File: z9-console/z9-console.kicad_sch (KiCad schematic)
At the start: 4 parts

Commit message: x
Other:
- sheet buzzer: file ../z9-shared/buzzer.kicad_sch -> ../z9-shared/shared_buzzer.kicad_sch
- sheet usbc: file ../z9-shared/usbc.kicad_sch -> ../z9-shared/shared_usbc.kicad_sch
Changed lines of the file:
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@@
 			)
 		)
-		(property "Sheetfile" "../z9-shared/buzzer.kicad_sch"
+		(property "Sheetfile" "../z9-shared/shared_buzzer.kicad_sch"
 			(at 299.72 85.6746 0)
 			(effects
@@
 			)
 		)
-		(property "Sheetfile" "../z9-shared/usbc.kicad_sch"
+		(property "Sheetfile" "../z9-shared/shared_usbc.kicad_sch"
 			(at 299.72 174.5746 0)
 			(effects

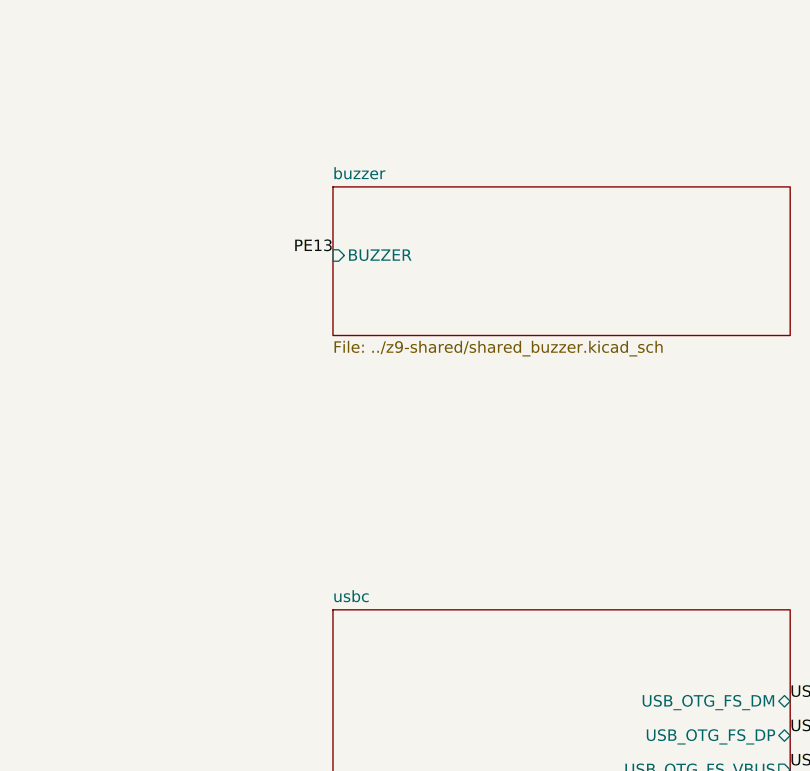
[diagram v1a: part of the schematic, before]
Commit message: lcd power switch-- add new accelerometer
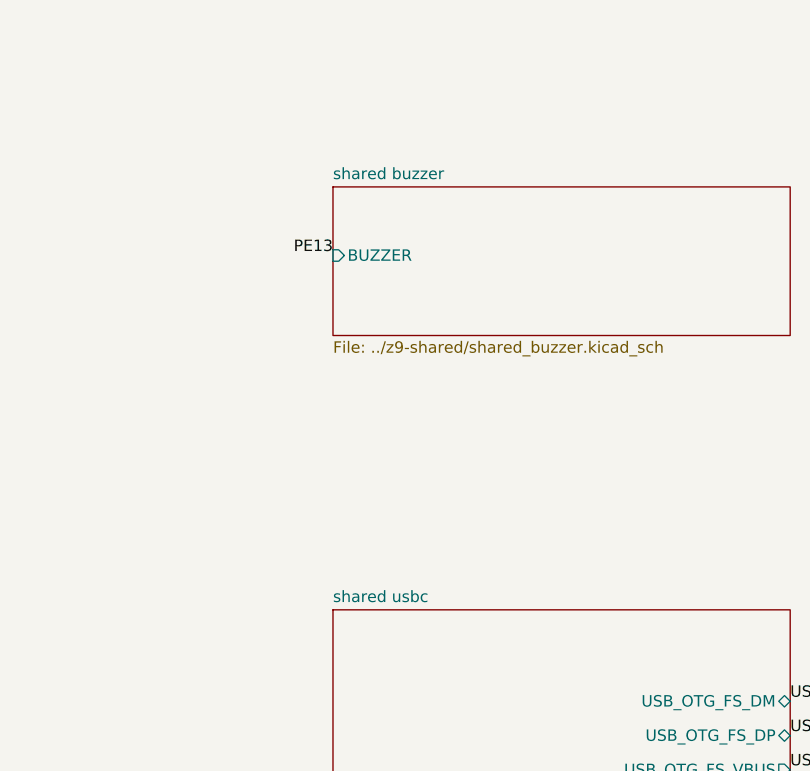
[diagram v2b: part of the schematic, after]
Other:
- sheet buzzer renamed shared buzzer
- sheet usbc renamed shared usbc
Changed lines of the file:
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@@
 			(color 0 0 0 0.0000)
 		)
-		(property "Sheetname" "buzzer"
+		(property "Sheetname" "shared buzzer"
 			(at 299.72 67.8684 0)
 			(effects
@@
 			(color 0 0 0 0.0000)
 		)
-		(property "Sheetname" "usbc"
+		(property "Sheetname" "shared usbc"
 			(at 299.72 114.8584 0)
 			(effects

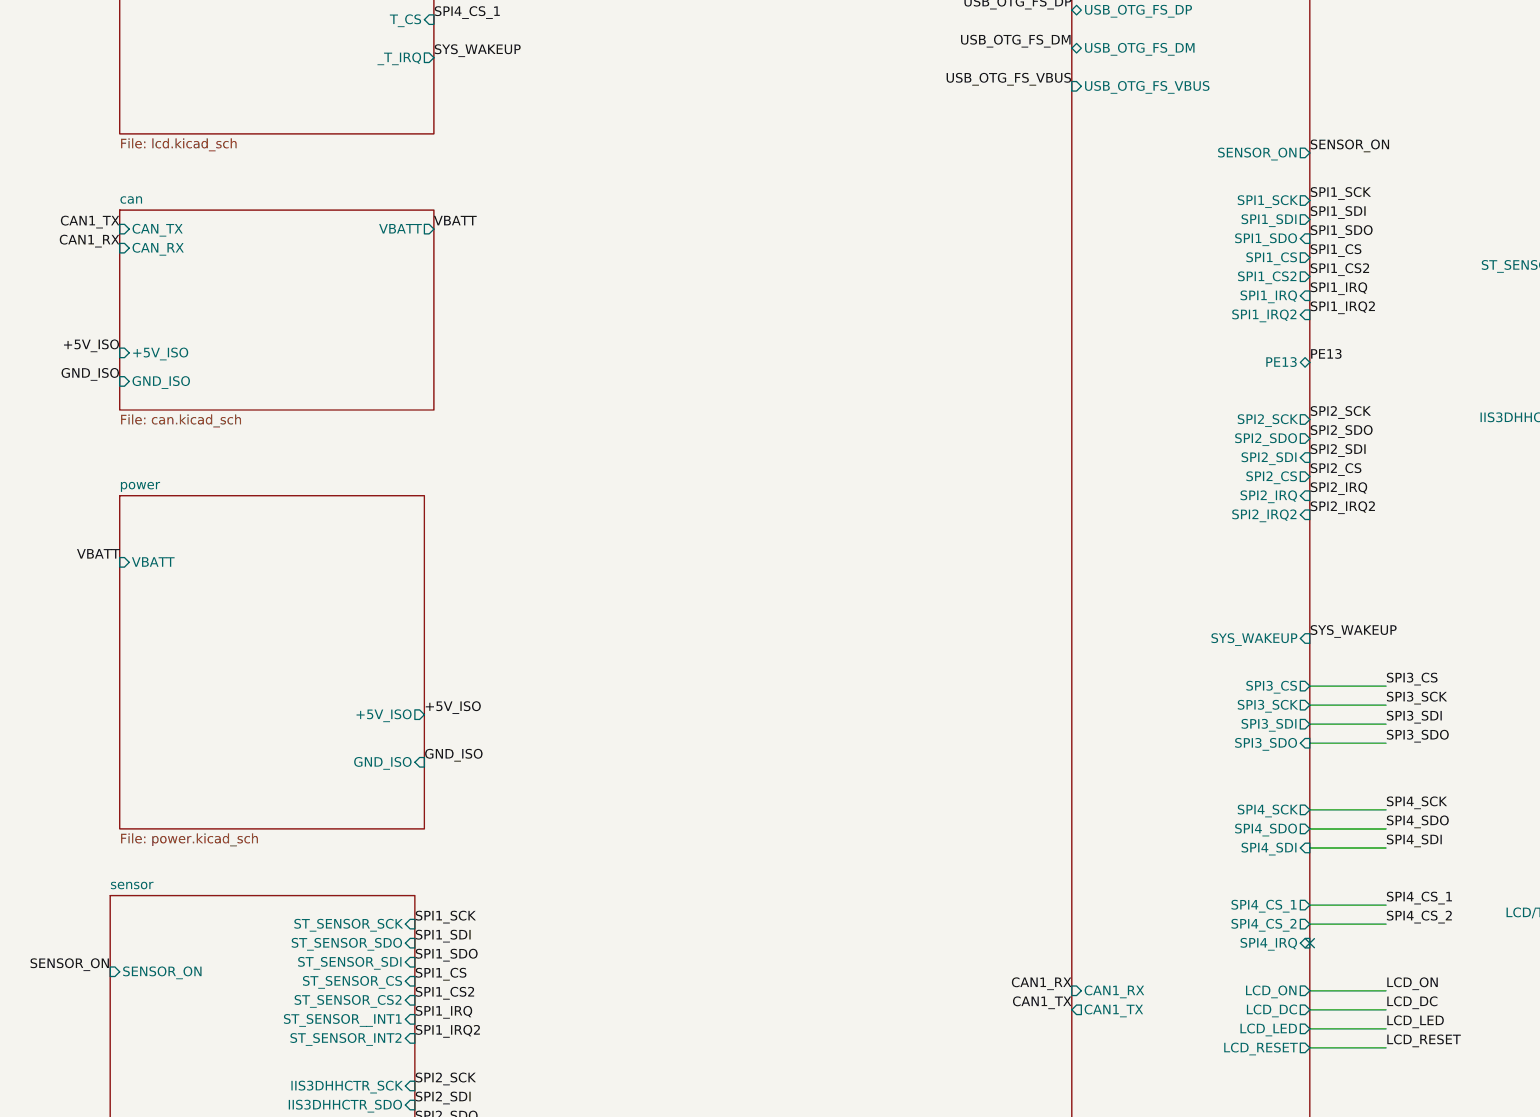
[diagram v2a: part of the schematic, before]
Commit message: change MEMS device
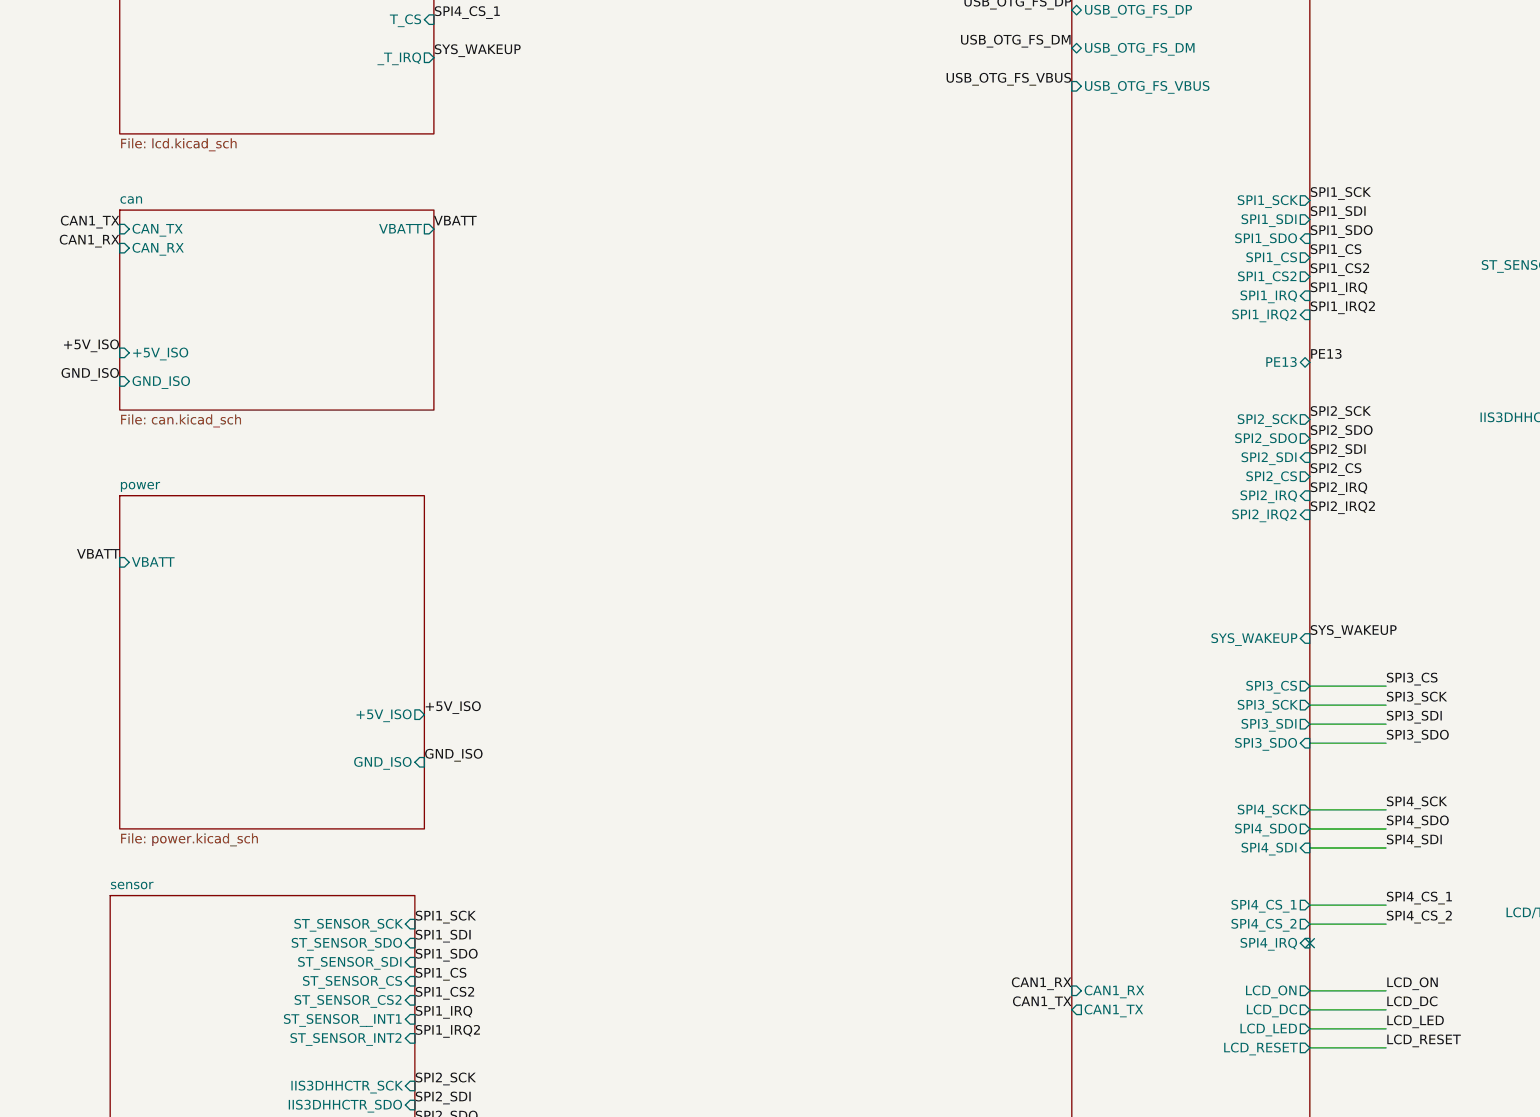
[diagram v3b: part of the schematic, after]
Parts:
- renumbered H2 to H901, H3 to H902, H1 to H903, H4 to H904
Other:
- sheet MCU ports: added none; removed SENSOR_ON
- sheet sensor ports: added none; removed SENSOR_ON
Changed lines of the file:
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@@
-		)
-	)
-	(label "SENSOR_ON"
-		(at 212.09 113.03 0)
-		(effects
-			(font
-				(size 1.27 1.27)
-			)
-			(justify left bottom)
 		)
 	)
@@
 		)
 	)
-	(label "SENSOR_ON"
-		(at 52.07 222.25 180)
-		(effects
-			(font
-				(size 1.27 1.27)
-			)
-			(justify right bottom)
-		)
-	)
 	(label "SPI1_SCK"
 		(at 212.09 119.38 0)
@@
 	)
 	(symbol
-		(lib_name "MountingHole_3")
 		(lib_id "Mechanical:MountingHole")
 		(at 388.62 245.11 0)
@@
 		(dnp no)
 		(fields_autoplaced yes)
-		(property "Reference" "H2"
+		(property "Reference" "H901"
 			(at 391.16 243.8399 0)
 			(effects
@@
 			(project "l8-kicad"
 				(path "/8d063f79-9282-4820-bcf4-1ff3c006cf08"
-					(reference "H2")
+					(reference "H901")
 					(unit 1)
 				)
@@
 	)
 	(symbol
-		(lib_name "MountingHole_1")
 		(lib_id "Mechanical:MountingHole")
 		(at 393.7 245.11 0)
@@
 		(dnp no)
 		(fields_autoplaced yes)
-		(property "Reference" "H3"
+		(property "Reference" "H902"
 			(at 396.24 243.8399 0)
 			(effects
@@
 			(project "l8-kicad"
 				(path "/8d063f79-9282-4820-bcf4-1ff3c006cf08"
-					(reference "H3")
+					(reference "H902")
 					(unit 1)
 				)
@@
 	)
 	(symbol
-		(lib_name "MountingHole_2")
 		(lib_id "Mechanical:MountingHole")
 		(at 398.78 245.11 0)
@@
 		(dnp no)
 		(fields_autoplaced yes)
-		(property "Reference" "H1"
+		(property "Reference" "H903"
 			(at 401.32 243.8399 0)
 			(effects
@@
 			(project "l8-kicad"
 				(path "/8d063f79-9282-4820-bcf4-1ff3c006cf08"
-					(reference "H1")
+					(reference "H903")
 					(unit 1)
 				)
@@
 		(dnp no)
 		(fields_autoplaced yes)
-		(property "Reference" "H4"
+		(property "Reference" "H904"
 			(at 406.4 243.8399 0)
 			(effects
@@
 			(project "l8-kicad"
 				(path "/8d063f79-9282-4820-bcf4-1ff3c006cf08"
-					(reference "H4")
+					(reference "H904")
 					(unit 1)
 				)
@@
 			)
 		)
-		(pin "SENSOR_ON" output
-			(at 212.09 113.03 0)
-			(effects
-				(font
-					(size 1.27 1.27)
-				)
-				(justify right)
-			)
-		)
 		(pin "LCD_DC" output
 			(at 212.09 227.33 0)
@@
 			)
 		)
-		(pin "SENSOR_ON" input
-			(at 52.07 222.25 180)
-			(effects
-				(font
-					(size 1.27 1.27)
-				)
-				(justify left)
-			)
-		)

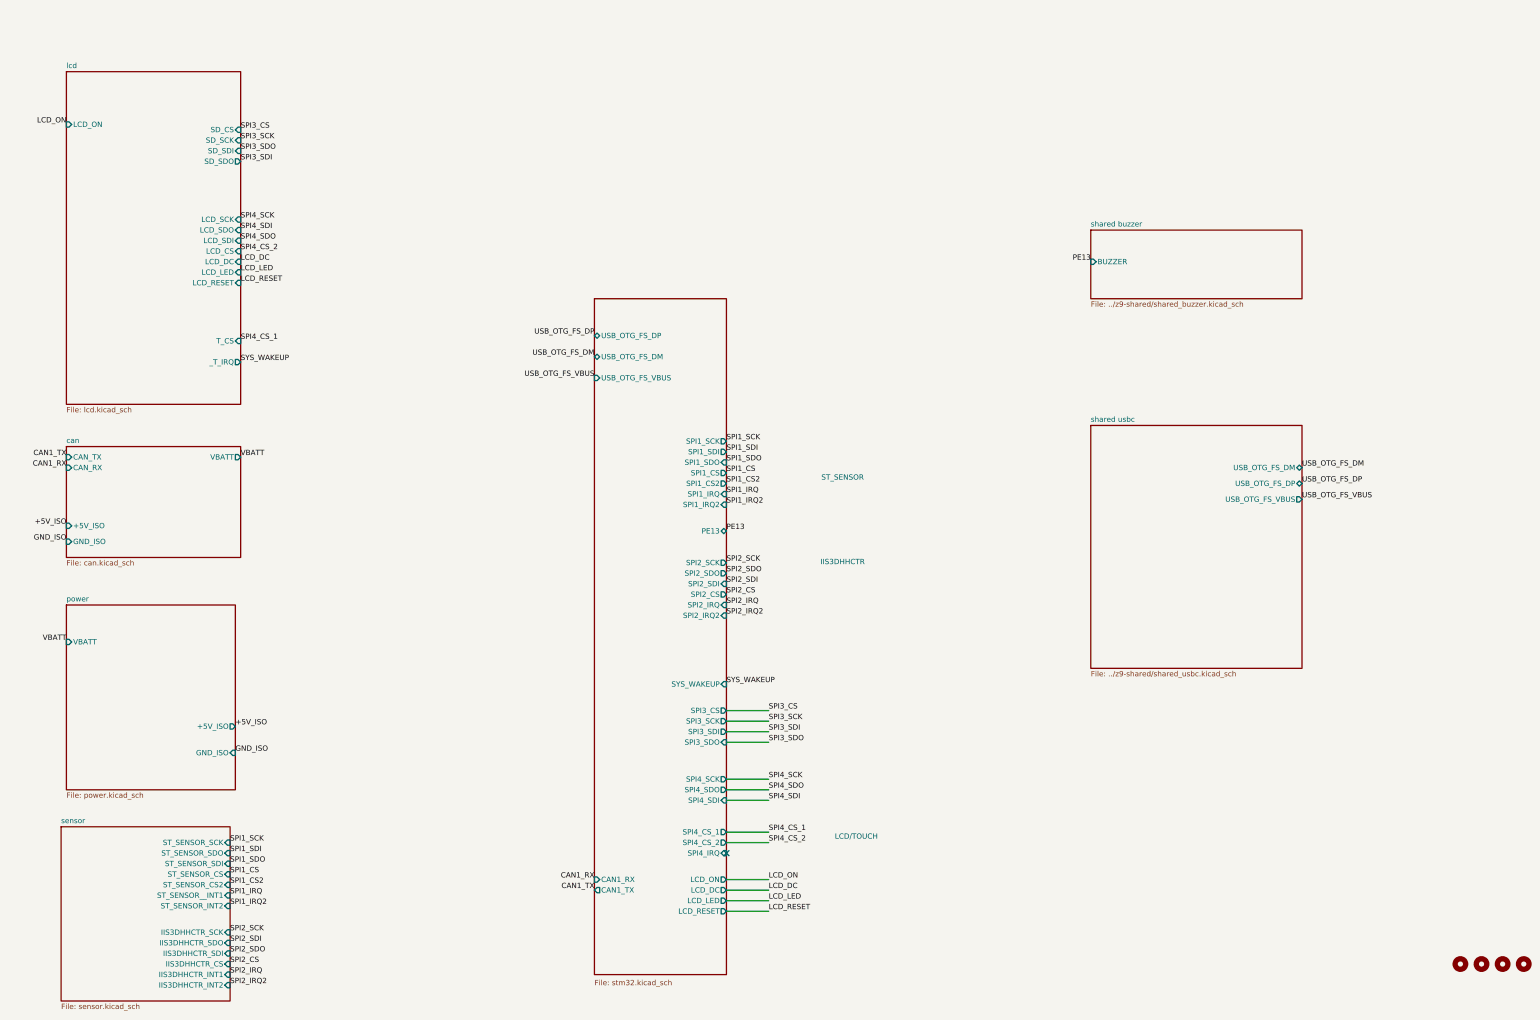
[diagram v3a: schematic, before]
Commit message: annotation issues on shared schematics
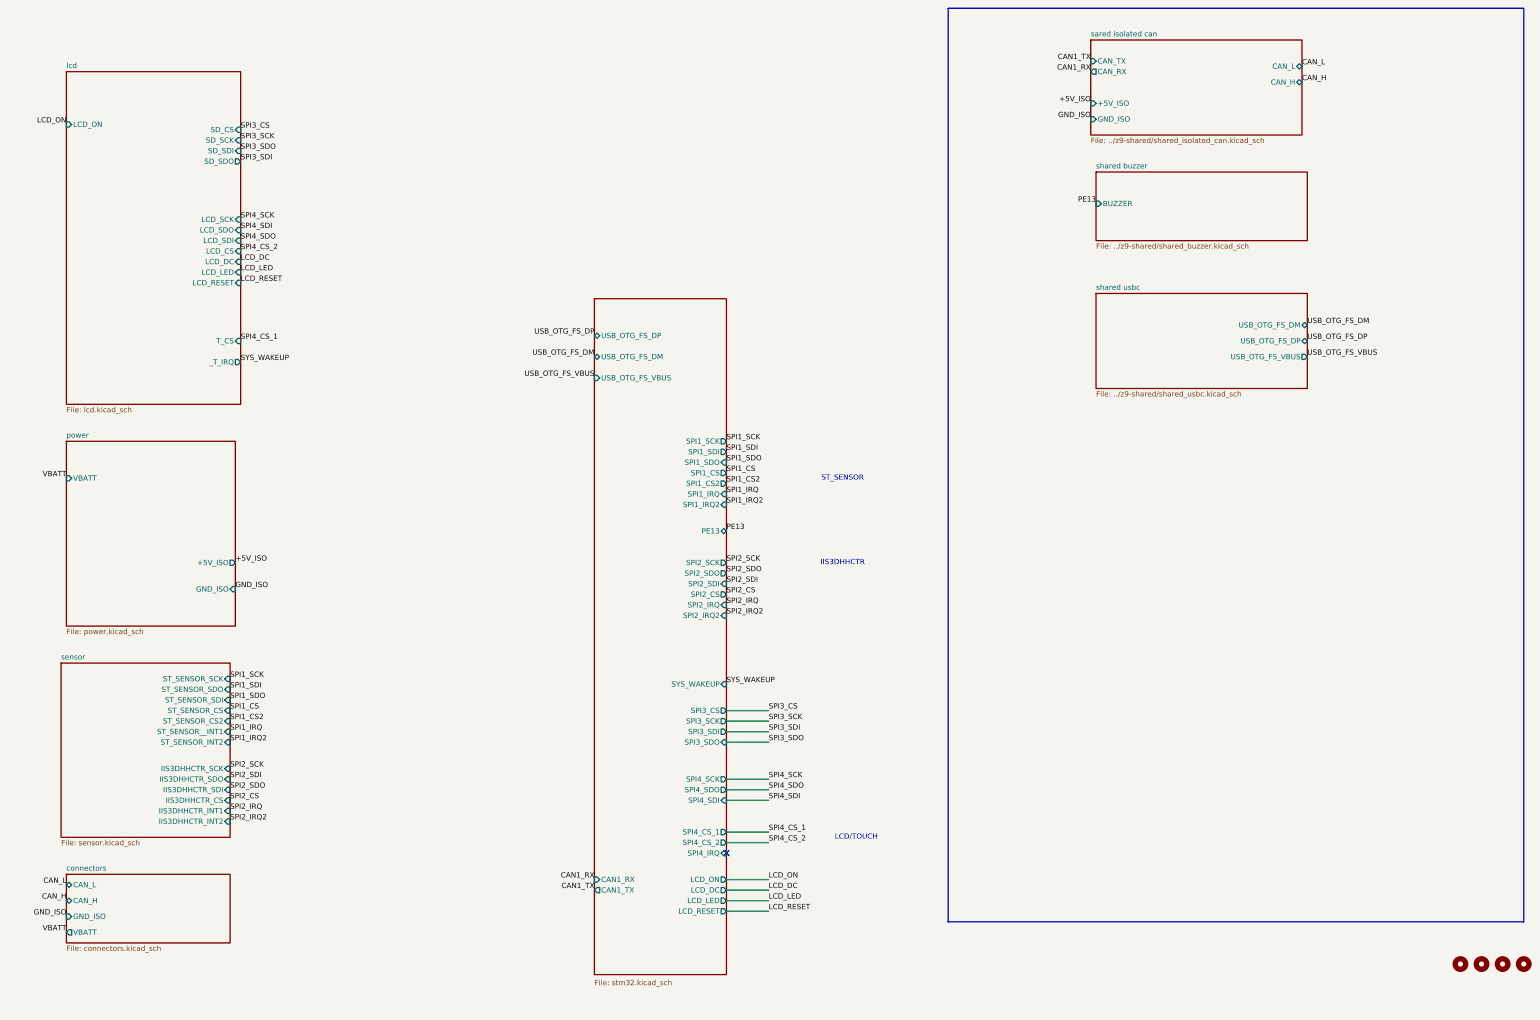
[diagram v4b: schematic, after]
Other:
- removed sheet can
- added sheet connectors (connectors.kicad_sch)
- added sheet sared isolated can (../z9-shared/shared_isolated_can.kicad_sch)

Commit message: another reannotate
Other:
- sheet sared isolated can renamed shared isolated can
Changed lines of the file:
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@@
 			(project "z9-console"
 				(path "/8d063f79-9282-4820-bcf4-1ff3c006cf08"
-					(page "8")
+					(page "700")
 				)
 			)
@@
 			(project "z9-console"
 				(path "/8d063f79-9282-4820-bcf4-1ff3c006cf08"
-					(page "8")
+					(page "800")
 				)
 			)
@@
 			(color 0 0 0 0.0000)
 		)
-		(property "Sheetname" "sared isolated can"
+		(property "Sheetname" "shared isolated can"
 			(at 299.72 22.1484 0)
 			(effects
@@
 			(project "z9-console"
 				(path "/8d063f79-9282-4820-bcf4-1ff3c006cf08"
-					(page "9")
-				)
-			)
+					(page "950")
+				)
+			)
